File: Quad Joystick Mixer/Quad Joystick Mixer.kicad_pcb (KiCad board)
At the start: 2 copper layers, 55 x 96.8 mm, 59 parts, among them J1 B6B-XH-A, J2 Barrel_Jack_Switch, SW1 SW_DPDT_x2, U1 LM338-TO-220, U2 LM2990T-12/NOPB, U3 AP63200WU

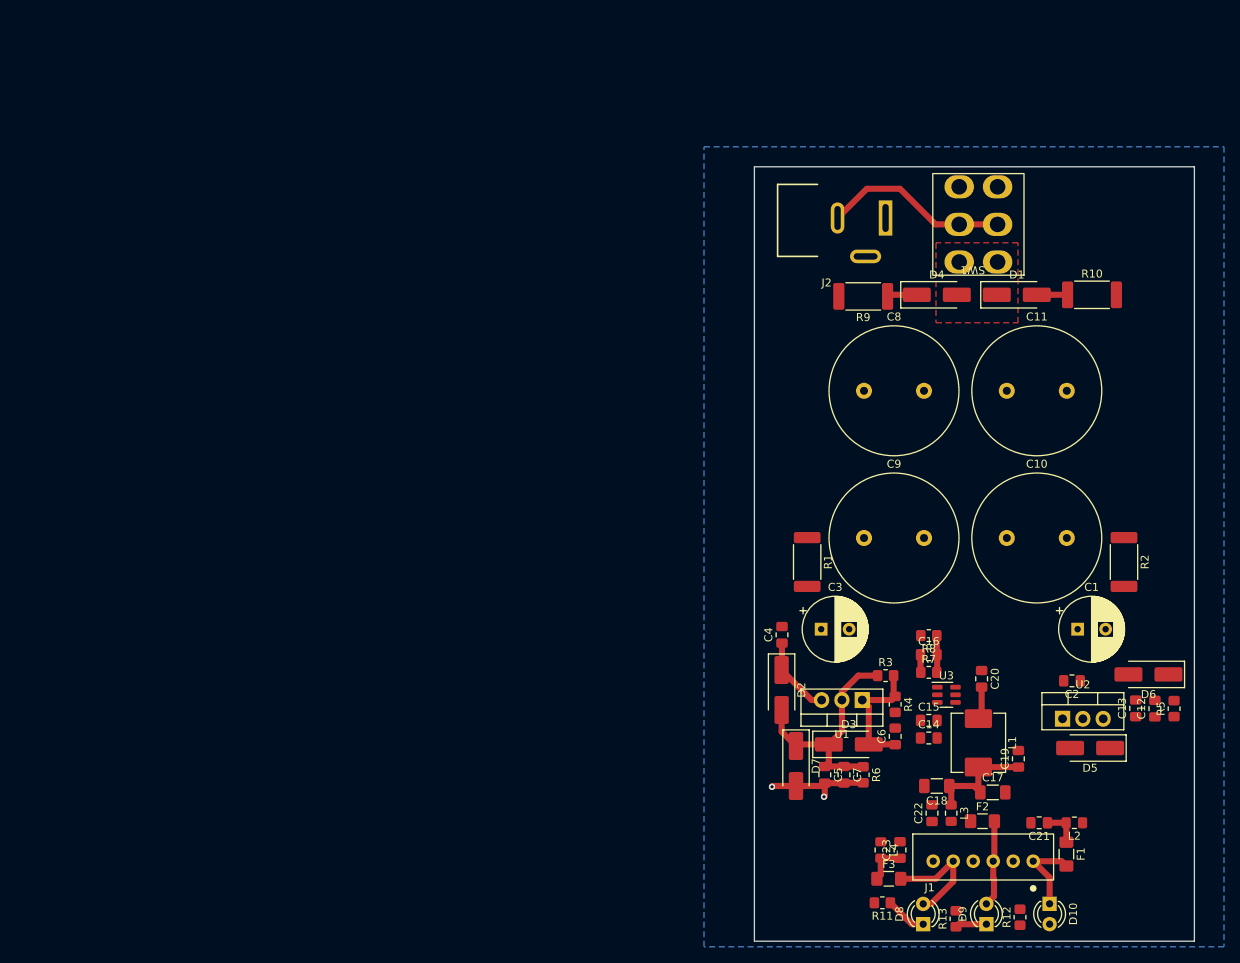
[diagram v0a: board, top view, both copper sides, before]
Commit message: clean up power supply schematic
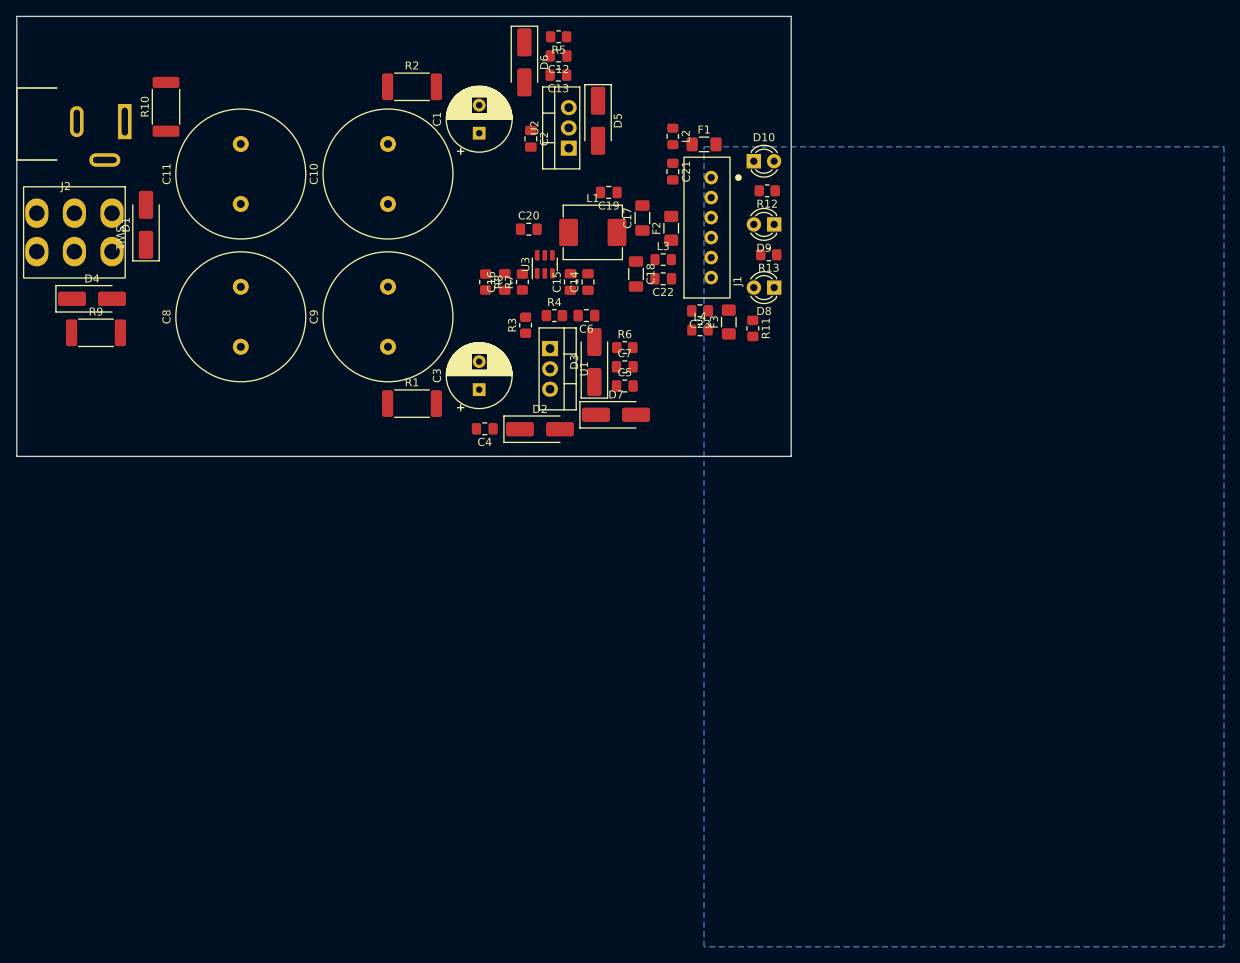
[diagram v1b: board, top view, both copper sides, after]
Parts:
- moved R10 118.1 mm to (55.2, 42.5), turned to 90 degrees
- moved R5 113.9 mm to (104.3, 33.7), turned to 180 degrees
- moved SW1 113.0 mm to (43.8, 58.2), turned to -90 degrees
- moved C12 110.5 mm to (104.3, 36.1), turned to 180 degrees
- moved D6 109.3 mm to (100.1, 36.9), turned to -90 degrees
- moved D1 109.2 mm to (52.8, 57.2), turned to 90 degrees
- moved C13 107.1 mm to (104.3, 38.5), turned to 180 degrees
- moved R2 107.0 mm to (86.0, 40.0), turned to 0 degrees
- moved D4 105.6 mm to (46.0, 66.5)
- moved D10 99.9 mm to (128.7, 49.3), turned to 0 degrees
- moved D5 99.7 mm to (109.3, 44.2), turned to -90 degrees
- moved F1 99.6 mm to (122.5, 47.2), turned to 0 degrees
- moved L2 99.4 mm to (118.6, 46.2), turned to -90 degrees
- moved C11 98.6 mm to (64.6, 54.6), turned to 90 degrees
- moved C1 97.2 mm to (94.4, 45.8), turned to 90 degrees
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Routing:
- net +12V: track 29.8 -> 0.00 mm
- net Net-(SW1A-B): track 23.4 -> 0.00 mm
- net +5V: track 17.2 -> 0.00 mm
- net Net-(D3-A): track 16.2 -> 0.00 mm
- net Net-(D8-A): track 14.9 -> 0.00 mm
- net Earth: track 13.4 -> 0.00 mm, vias 2 -> 0
- net Net-(D9-A): track 10.8 -> 0.00 mm
- net Net-(D10-K): track 10.6 -> 0.00 mm
- net Net-(D2-K): track 9.94 -> 0.00 mm
- net Net-(D8-K): track 5.21 -> 0.00 mm
- net Net-(C23-Pad1): track 5.18 -> 0.00 mm
- net Net-(C21-Pad1): track 4.77 -> 0.00 mm
- net Net-(U3-FB): track 4.63 -> 0.00 mm
- net Net-(U3-SW): track 4.10 -> 0.00 mm
- net Net-(D9-K): track 3.93 -> 0.00 mm
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- removed copper zone on F.Cu, net Net-(D1-K)
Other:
- board size 55 x 96.8 mm -> 96.8 x 55 mm

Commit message: work on placement and layout
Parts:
- removed F1, F2, F3: Polyfuse, Fuse:Fuse_1206_3216Metric_Pad1.42x1.75mm_HandSolder
- removed L1: 10uH, Inductor_SMD:L_Abracon_ASPI-0630LR
- removed L2, L3: L_Ferrite, Inductor_SMD:L_0805_2012Metric_Pad1.15x1.40mm_HandSolder
- added C24: 1uF, Capacitor_SMD:C_0805_2012Metric_Pad1.18x1.45mm_HandSolder, F.Cu at (313.4, 83.0)
- added C25: 10pF, Capacitor_SMD:C_0805_2012Metric_Pad1.18x1.45mm_HandSolder, F.Cu at (334.9, 66.5)
- added C26: 10uF, Capacitor_SMD:C_0805_2012Metric_Pad1.18x1.45mm_HandSolder, F.Cu at (330.3, 74.7)
- added C27: 10pF, Capacitor_SMD:C_0805_2012Metric_Pad1.18x1.45mm_HandSolder, F.Cu at (346.4, 61.5)
- added C28: 1uF, Capacitor_SMD:C_0805_2012Metric_Pad1.18x1.45mm_HandSolder, F.Cu at (358.4, 85.0)
- added C29: 10uF, Capacitor_SMD:C_0805_2012Metric_Pad1.18x1.45mm_HandSolder, F.Cu at (338.8, 77.1)
- added C30: 0.1uF, Capacitor_SMD:C_0805_2012Metric_Pad1.18x1.45mm_HandSolder, F.Cu at (334.3, 77.1)
- added C31: 0.1uF, Capacitor_SMD:C_0805_2012Metric_Pad1.18x1.45mm_HandSolder, F.Cu at (338.3, 68.1)
- added C32: 1uF, Capacitor_SMD:C_0805_2012Metric_Pad1.18x1.45mm_HandSolder, F.Cu at (335.5, 121.9)
- added C33: 1uF, Capacitor_SMD:C_0805_2012Metric_Pad1.18x1.45mm_HandSolder, F.Cu at (338.0, 131.4)
- added C34: 0.1uF, Capacitor_SMD:C_0805_2012Metric_Pad1.18x1.45mm_HandSolder, F.Cu at (-151.1, 101.3)
- added C35: 0.1uF, Capacitor_SMD:C_0805_2012Metric_Pad1.18x1.45mm_HandSolder, F.Cu at (-151.1, 104.3)
- added C36: 0.1uF, Capacitor_SMD:C_0805_2012Metric_Pad1.18x1.45mm_HandSolder, F.Cu at (-151.1, 107.3)
- added C37: 1uF, Capacitor_SMD:C_0805_2012Metric_Pad1.18x1.45mm_HandSolder, F.Cu at (-146.3, 92.3)
- added C38: 0.1uF, Capacitor_SMD:C_0805_2012Metric_Pad1.18x1.45mm_HandSolder, F.Cu at (-146.3, 95.3)
- added C39: 0.1uF, Capacitor_SMD:C_0805_2012Metric_Pad1.18x1.45mm_HandSolder, F.Cu at (-146.3, 98.3)
- added C40: 0.1uF, Capacitor_SMD:C_0805_2012Metric_Pad1.18x1.45mm_HandSolder, F.Cu at (-146.3, 101.3)
- added C41: 0.1uF, Capacitor_SMD:C_0805_2012Metric_Pad1.18x1.45mm_HandSolder, F.Cu at (-146.3, 104.3)
- added C42: 0.1uF, Capacitor_SMD:C_0805_2012Metric_Pad1.18x1.45mm_HandSolder, F.Cu at (-146.3, 107.3)
- added C43: 0.1uF, Capacitor_SMD:C_0805_2012Metric_Pad1.18x1.45mm_HandSolder, F.Cu at (138.6, 31.3)
- added C44: 0.1uF, Capacitor_SMD:C_0805_2012Metric_Pad1.18x1.45mm_HandSolder, F.Cu at (141.6, 31.3)
- added C45: 1uF, Capacitor_SMD:C_0805_2012Metric_Pad1.18x1.45mm_HandSolder, F.Cu at (-141.5, 92.3)
- added C46: 1uF, Capacitor_SMD:C_0805_2012Metric_Pad1.18x1.45mm_HandSolder, F.Cu at (-141.5, 95.3)
- added C47: 1uF, Capacitor_SMD:C_0805_2012Metric_Pad1.18x1.45mm_HandSolder, F.Cu at (-141.5, 98.3)
- added C48: 1uF, Capacitor_SMD:C_0805_2012Metric_Pad1.18x1.45mm_HandSolder, F.Cu at (-141.5, 101.3)
- added C49: 330pF, Capacitor_SMD:C_0805_2012Metric_Pad1.18x1.45mm_HandSolder, F.Cu at (144.6, 31.3)
- added C50: 330pF, Capacitor_SMD:C_0805_2012Metric_Pad1.18x1.45mm_HandSolder, F.Cu at (147.6, 31.3)
- added C51: 330pF, Capacitor_SMD:C_0805_2012Metric_Pad1.18x1.45mm_HandSolder, F.Cu at (150.6, 31.3)
- added C52: 330pF, Capacitor_SMD:C_0805_2012Metric_Pad1.18x1.45mm_HandSolder, F.Cu at (153.6, 31.3)
- added C53: 0.1uF, Capacitor_SMD:C_0805_2012Metric_Pad1.18x1.45mm_HandSolder, F.Cu at (156.6, 31.3)
- added C54: 0.1uF, Capacitor_SMD:C_0805_2012Metric_Pad1.18x1.45mm_HandSolder, F.Cu at (159.6, 31.3)
- added C55: 1uF, Capacitor_SMD:C_0805_2012Metric_Pad1.18x1.45mm_HandSolder, F.Cu at (-151.1, 127.1)
- added C56: 0.1uF, Capacitor_SMD:C_0805_2012Metric_Pad1.18x1.45mm_HandSolder, F.Cu at (-61.5, 185.0)
- added C57: 0.1uF, Capacitor_SMD:C_0805_2012Metric_Pad1.18x1.45mm_HandSolder, F.Cu at (-61.5, 182.5)
- added C58: 1uF, Capacitor_SMD:C_0805_2012Metric_Pad1.18x1.45mm_HandSolder, F.Cu at (-151.1, 136.1)
- added C59: 1uF, Capacitor_SMD:C_0805_2012Metric_Pad1.18x1.45mm_HandSolder, F.Cu at (-151.1, 139.1)
- added C60: 0.1uF, Capacitor_SMD:C_0805_2012Metric_Pad1.18x1.45mm_HandSolder, F.Cu at (-151.1, 142.1)
- added C61: 0.1uF, Capacitor_SMD:C_0805_2012Metric_Pad1.18x1.45mm_HandSolder, F.Cu at (-146.3, 127.1)
- added C62: 0.1uF, Capacitor_SMD:C_0805_2012Metric_Pad1.18x1.45mm_HandSolder, F.Cu at (-146.3, 130.1)
- added C63: 0.1uF, Capacitor_SMD:C_0805_2012Metric_Pad1.18x1.45mm_HandSolder, F.Cu at (-146.3, 133.1)
- added C64: 0.1uF, Capacitor_SMD:C_0805_2012Metric_Pad1.18x1.45mm_HandSolder, F.Cu at (-146.3, 136.1)
- added C65: 1uF, Capacitor_SMD:C_0805_2012Metric_Pad1.18x1.45mm_HandSolder, F.Cu at (-146.3, 139.1)
- added C66: 1uF, Capacitor_SMD:C_0805_2012Metric_Pad1.18x1.45mm_HandSolder, F.Cu at (-146.3, 142.1)
- added C67: 0.1uF, Capacitor_SMD:C_0805_2012Metric_Pad1.18x1.45mm_HandSolder, F.Cu at (-72.5, 199.0)
- added C68: 0.1uF, Capacitor_SMD:C_0805_2012Metric_Pad1.18x1.45mm_HandSolder, F.Cu at (-141.5, 130.1)
- added C69: 0.1uF, Capacitor_SMD:C_0805_2012Metric_Pad1.18x1.45mm_HandSolder, F.Cu at (-76.5, 207.0)
- added C70: 0.1uF, Capacitor_SMD:C_0805_2012Metric_Pad1.18x1.45mm_HandSolder, F.Cu at (-141.5, 136.1)
- added C71: 0.1uF, Capacitor_SMD:C_0805_2012Metric_Pad1.18x1.45mm_HandSolder, F.Cu at (51.6, 237.8)
- added C72: 0.1uF, Capacitor_SMD:C_0805_2012Metric_Pad1.18x1.45mm_HandSolder, F.Cu at (43.6, 233.8)
- added C73: 0.1uF, Capacitor_SMD:C_0805_2012Metric_Pad1.18x1.45mm_HandSolder, F.Cu at (39.5, 246.8)
- added C74: 0.1uF, Capacitor_SMD:C_0805_2012Metric_Pad1.18x1.45mm_HandSolder, F.Cu at (40.0, 232.3)
- added C75: 10uF, Capacitor_SMD:C_0805_2012Metric_Pad1.18x1.45mm_HandSolder, F.Cu at (42.5, 228.3)
- added C76: 10uF, Capacitor_SMD:C_0805_2012Metric_Pad1.18x1.45mm_HandSolder, F.Cu at (42.0, 242.8)
- added C77: 0.1uF, Capacitor_SMD:C_0805_2012Metric_Pad1.18x1.45mm_HandSolder, F.Cu at (113.2, 84.1)
- added C78: 0.1uF, Capacitor_SMD:C_0805_2012Metric_Pad1.18x1.45mm_HandSolder, F.Cu at (113.2, 88.3)
- added C80: 0.1uF, Capacitor_SMD:C_0805_2012Metric_Pad1.18x1.45mm_HandSolder, F.Cu at (100.9, 120.6)
- added C81: 0.1uF, Capacitor_SMD:C_0805_2012Metric_Pad1.18x1.45mm_HandSolder, F.Cu at (-8.68, 23.1)
- added C82: 0.1uF, Capacitor_SMD:C_0805_2012Metric_Pad1.18x1.45mm_HandSolder, F.Cu at (71.6, 224.0)
- added C83: 0.1uF, Capacitor_SMD:C_0805_2012Metric_Pad1.18x1.45mm_HandSolder, F.Cu at (93.6, 224.0)
- added C84: 0.1uF, Capacitor_SMD:C_0805_2012Metric_Pad1.18x1.45mm_HandSolder, F.Cu at (113.0, 224.0)
- added C85: 0.1uF, Capacitor_SMD:C_0805_2012Metric_Pad1.18x1.45mm_HandSolder, F.Cu at (109.0, 120.8)
- added C86: 0.1uF, Capacitor_SMD:C_0805_2012Metric_Pad1.18x1.45mm_HandSolder, F.Cu at (105.0, 121.5)
- added D11: LED, LED_THT:LED_D3.0mm_FlatTop, F.Cu at (-124.2, 38.0)
- added D12: MMSZ5222BT1G, Diode_SMD:D_SOD-123, F.Cu at (311.4, 73.5)
- added D13: MMSZ5222BT1G, Diode_SMD:D_SOD-123, F.Cu at (308.4, 73.5)
- added D14: MMSZ5222BT1G, Diode_SMD:D_SOD-123, F.Cu at (359.9, 71.0)
- added D15: MMSZ5222BT1G, Diode_SMD:D_SOD-123, F.Cu at (359.9, 76.5)
- added D16: BZT52C4V7-13-F, Diode_SMD:D_SOD-123, F.Cu at (-127.7, 118.1)
- added D17: BZT52C4V7-13-F, Diode_SMD:D_SOD-123, F.Cu at (-127.7, 152.9)
- added D18: DDZ9684-7, Diode_SMD:D_SOD-123, F.Cu at (52.0, 233.0)
- added D19: DDZ9684-7, Diode_SMD:D_SOD-123, F.Cu at (50.0, 241.3)
- added D20: LED, LED_THT:LED_D3.0mm_FlatTop, F.Cu at (-20.3, 68.7)
- added D21: LED, LED_THT:LED_D3.0mm_FlatTop, F.Cu at (-20.3, 74.2)
- added D22: SMAJ5.0A, Diode_SMD:D_SMA, F.Cu at (71.6, 227.0)
- added D23: SMAJ5.0A, Diode_SMD:D_SMA, F.Cu at (93.6, 227.0)
- added D24: SMAJ5.0A, Diode_SMD:D_SMA, F.Cu at (113.0, 227.0)
- added D25: SMAJ5.0A, Diode_SMD:D_SMA, F.Cu at (105.5, 54.7)
- added D26: SMAJ5.0A, Diode_SMD:D_SMA, F.Cu at (89.0, 55.0)
- added J3: NMJ6HCD, Eyewool Connectors:NMJ6HCD, F.Cu at (346.9, 103.0)
- added J4: NMJ6HCD, Eyewool Connectors:NMJ6HCD, F.Cu at (147.4, 37.3)
- added J5: NMJ6HCD, Eyewool Connectors:NMJ6HCD, F.Cu at (168.0, 37.3)
- added J6: NMJ6HCD, Eyewool Connectors:NMJ6HCD, F.Cu at (188.6, 37.3)
- added J7: NMJ6HCD, Eyewool Connectors:NMJ6HCD, F.Cu at (209.2, 37.3)
- added NT1: NetTie_2, NetTie:NetTie-2_SMD_Pad2.0mm, F.Cu at (-111.9, 131.3)
- added Q1: 2N7002, Package_TO_SOT_SMD:SOT-23, F.Cu at (-10.1, 68.1)
- added Q2: 2N7002, Package_TO_SOT_SMD:SOT-23, F.Cu at (-10.1, 72.6)
- added R14: 100k, Resistor_SMD:R_0805_2012Metric_Pad1.20x1.40mm_HandSolder, F.Cu at (310.9, 83.0)
- added R15: 4.7k, Resistor_SMD:R_0805_2012Metric_Pad1.20x1.40mm_HandSolder, F.Cu at (330.3, 70.6)
- added R16: 470, Resistor_SMD:R_0805_2012Metric_Pad1.20x1.40mm_HandSolder, F.Cu at (332.4, 66.5)
- added R17: 470, Resistor_SMD:R_0805_2012Metric_Pad1.20x1.40mm_HandSolder, F.Cu at (346.4, 64.0)
- added R18: 4.7k, Resistor_SMD:R_0805_2012Metric_Pad1.20x1.40mm_HandSolder, F.Cu at (359.4, 81.5)
- added R19: 100k, Resistor_SMD:R_0805_2012Metric_Pad1.20x1.40mm_HandSolder, F.Cu at (360.9, 85.0)
- added R20: 4.7R, Resistor_SMD:R_2010_5025Metric_Pad1.40x2.65mm_HandSolder, F.Cu at (335.0, 132.9)
- added R21: 10k, Resistor_SMD:R_0805_2012Metric_Pad1.20x1.40mm_HandSolder, F.Cu at (339.2, 128.2)
- added R22: 10k, Resistor_SMD:R_0805_2012Metric_Pad1.20x1.40mm_HandSolder, F.Cu at (339.2, 124.4)
- added R23: 20k, Resistor_SMD:R_0805_2012Metric_Pad1.20x1.40mm_HandSolder, F.Cu at (-151.1, 113.3)
- added R24: 100k, Resistor_SMD:R_0805_2012Metric_Pad1.20x1.40mm_HandSolder, F.Cu at (-151.1, 116.2)
- added R25: 10k, Resistor_SMD:R_0805_2012Metric_Pad1.20x1.40mm_HandSolder, F.Cu at (-151.1, 119.2)
- added R26: 10k, Resistor_SMD:R_0805_2012Metric_Pad1.20x1.40mm_HandSolder, F.Cu at (-151.1, 122.1)
- added R27: 10k, Resistor_SMD:R_0805_2012Metric_Pad1.20x1.40mm_HandSolder, F.Cu at (-146.4, 110.3)
- added R28: 100k, Resistor_SMD:R_0805_2012Metric_Pad1.20x1.40mm_HandSolder, F.Cu at (-146.4, 113.3)
- added R29: 100k, Resistor_SMD:R_0805_2012Metric_Pad1.20x1.40mm_HandSolder, F.Cu at (-146.4, 116.2)
- added R30: 100k, Resistor_SMD:R_0805_2012Metric_Pad1.20x1.40mm_HandSolder, F.Cu at (-146.4, 119.2)
- added R31: 100k, Resistor_SMD:R_0805_2012Metric_Pad1.20x1.40mm_HandSolder, F.Cu at (-146.4, 122.1)
- added R32: 20k, Resistor_SMD:R_0805_2012Metric_Pad1.20x1.40mm_HandSolder, F.Cu at (162.6, 31.4)
- added R33: 20k, Resistor_SMD:R_0805_2012Metric_Pad1.20x1.40mm_HandSolder, F.Cu at (165.6, 31.4)
- added R34: 1k, Resistor_SMD:R_0805_2012Metric_Pad1.20x1.40mm_HandSolder, F.Cu at (168.5, 31.4)
- added R35: 1k, Resistor_SMD:R_0805_2012Metric_Pad1.20x1.40mm_HandSolder, F.Cu at (171.5, 31.4)
- added R36: 20k, Resistor_SMD:R_0805_2012Metric_Pad1.20x1.40mm_HandSolder, F.Cu at (174.4, 31.4)
- added R37: 20k, Resistor_SMD:R_0805_2012Metric_Pad1.20x1.40mm_HandSolder, F.Cu at (177.4, 31.4)
- added R38: 1k, Resistor_SMD:R_0805_2012Metric_Pad1.20x1.40mm_HandSolder, F.Cu at (180.3, 31.4)
- added R39: 1k, Resistor_SMD:R_0805_2012Metric_Pad1.20x1.40mm_HandSolder, F.Cu at (183.3, 31.4)
- added R40: DNA, Resistor_SMD:R_2010_5025Metric_Pad1.40x2.65mm_HandSolder, F.Cu at (-111.5, 127.7)
- added R44: 10k, Resistor_SMD:R_0805_2012Metric_Pad1.20x1.40mm_HandSolder, F.Cu at (-141.6, 110.3)
- added R45: 10k, Resistor_SMD:R_0805_2012Metric_Pad1.20x1.40mm_HandSolder, F.Cu at (-141.6, 113.3)
- added R46: 10k, Resistor_SMD:R_0805_2012Metric_Pad1.20x1.40mm_HandSolder, F.Cu at (-141.6, 116.2)
- added R47: 10k, Resistor_SMD:R_0805_2012Metric_Pad1.20x1.40mm_HandSolder, F.Cu at (-141.6, 119.2)
- added R48: 100k, Resistor_SMD:R_0805_2012Metric_Pad1.20x1.40mm_HandSolder, F.Cu at (-151.1, 145.1)
- added R49: 10k, Resistor_SMD:R_0805_2012Metric_Pad1.20x1.40mm_HandSolder, F.Cu at (-151.1, 148.1)
- added R50: 100k, Resistor_SMD:R_0805_2012Metric_Pad1.20x1.40mm_HandSolder, F.Cu at (-151.1, 151.0)
- added R51: 10k, Resistor_SMD:R_0805_2012Metric_Pad1.20x1.40mm_HandSolder, F.Cu at (-61.5, 189.0)
- added R52: 10k, Resistor_SMD:R_0805_2012Metric_Pad1.20x1.40mm_HandSolder, F.Cu at (-151.1, 156.9)
- added R53: 100k, Resistor_SMD:R_0805_2012Metric_Pad1.20x1.40mm_HandSolder, F.Cu at (-146.4, 145.1)
- added R54: 20k, Resistor_SMD:R_0805_2012Metric_Pad1.20x1.40mm_HandSolder, F.Cu at (-146.4, 148.1)
- added R55: 20k, Resistor_SMD:R_0805_2012Metric_Pad1.20x1.40mm_HandSolder, F.Cu at (-146.4, 151.0)
- added R56: 10k, Resistor_SMD:R_0805_2012Metric_Pad1.20x1.40mm_HandSolder, F.Cu at (-146.4, 154.0)
- added R57: 10k, Resistor_SMD:R_0805_2012Metric_Pad1.20x1.40mm_HandSolder, F.Cu at (-146.4, 156.9)
- added R58: 100k, Resistor_SMD:R_0805_2012Metric_Pad1.20x1.40mm_HandSolder, F.Cu at (-141.6, 145.1)
- added R59: 10k, Resistor_SMD:R_0805_2012Metric_Pad1.20x1.40mm_HandSolder, F.Cu at (-141.6, 148.1)
- added R60: 10k, Resistor_SMD:R_0805_2012Metric_Pad1.20x1.40mm_HandSolder, F.Cu at (-141.6, 151.0)
- added R61: 100k, Resistor_SMD:R_0805_2012Metric_Pad1.20x1.40mm_HandSolder, F.Cu at (-141.6, 154.0)
- added R62: 1.43k, Resistor_SMD:R_0805_2012Metric_Pad1.20x1.40mm_HandSolder, F.Cu at (155.1, 243.3)
- added R63: 3.32k, Resistor_SMD:R_0805_2012Metric_Pad1.20x1.40mm_HandSolder, F.Cu at (151.1, 246.8)
- added R64: 100, Resistor_SMD:R_0805_2012Metric_Pad1.20x1.40mm_HandSolder, F.Cu at (40.0, 228.3)
- added R65: 100, Resistor_SMD:R_0805_2012Metric_Pad1.20x1.40mm_HandSolder, F.Cu at (39.5, 242.8)
- added R66: 4.7k, Resistor_SMD:R_0805_2012Metric_Pad1.20x1.40mm_HandSolder, F.Cu at (115.7, 100.8)
- added R67: 4.7k, Resistor_SMD:R_0805_2012Metric_Pad1.20x1.40mm_HandSolder, F.Cu at (115.7, 104.3)
- added R68: 4.7k, Resistor_SMD:R_0805_2012Metric_Pad1.20x1.40mm_HandSolder, F.Cu at (115.7, 107.8)
- added R69: 4.7k, Resistor_SMD:R_0805_2012Metric_Pad1.20x1.40mm_HandSolder, F.Cu at (115.7, 111.1)
- added R72: 10k, Resistor_SMD:R_0805_2012Metric_Pad1.20x1.40mm_HandSolder, F.Cu at (-19.6, 61.5)
- added R73: 6.04k, Resistor_SMD:R_0805_2012Metric_Pad1.20x1.40mm_HandSolder, F.Cu at (143.6, 248.3)
- added R74: 10k, Resistor_SMD:R_0805_2012Metric_Pad1.20x1.40mm_HandSolder, F.Cu at (135.6, 243.8)
- added R75: 16.5k, Resistor_SMD:R_0805_2012Metric_Pad1.20x1.40mm_HandSolder, F.Cu at (134.1, 236.3)
- added R76: 30.1k, Resistor_SMD:R_0805_2012Metric_Pad1.20x1.40mm_HandSolder, F.Cu at (138.1, 227.3)
- added R77: 71.5k, Resistor_SMD:R_0805_2012Metric_Pad1.20x1.40mm_HandSolder, F.Cu at (152.1, 227.8)
- added R78: 200, Resistor_SMD:R_0805_2012Metric_Pad1.20x1.40mm_HandSolder, F.Cu at (-14.8, 61.5)
- added R79: 10k, Resistor_SMD:R_0805_2012Metric_Pad1.20x1.40mm_HandSolder, F.Cu at (-14.8, 64.4)
- added R80: 200, Resistor_SMD:R_0805_2012Metric_Pad1.20x1.40mm_HandSolder, F.Cu at (-10.1, 49.7)
- added R81: 10k, Resistor_SMD:R_0805_2012Metric_Pad1.20x1.40mm_HandSolder, F.Cu at (-10.1, 52.6)
- added R82: 10k, Resistor_SMD:R_0805_2012Metric_Pad1.20x1.40mm_HandSolder, F.Cu at (75.1, 223.0)
- added R83: 10k, Resistor_SMD:R_0805_2012Metric_Pad1.20x1.40mm_HandSolder, F.Cu at (97.1, 223.0)
- added R84: 10k, Resistor_SMD:R_0805_2012Metric_Pad1.20x1.40mm_HandSolder, F.Cu at (116.5, 223.0)
- added R85: DNA, Resistor_SMD:R_0805_2012Metric_Pad1.20x1.40mm_HandSolder, F.Cu at (-117.8, 127.1)
- added R86: DNA, Resistor_SMD:R_0805_2012Metric_Pad1.20x1.40mm_HandSolder, F.Cu at (-117.8, 130.0)
- added R87: DNA, Resistor_SMD:R_0805_2012Metric_Pad1.20x1.40mm_HandSolder, F.Cu at (-117.8, 133.0)
- added R88: DNA, Resistor_SMD:R_0805_2012Metric_Pad1.20x1.40mm_HandSolder, F.Cu at (-117.8, 135.9)
- added RV1: 500kA, Eyewool Pots:StomboxParts_9MM, F.Cu at (321.9, 71.5)
- added RV2: 500kA, Eyewool Pots:StomboxParts_9MM, F.Cu at (349.4, 72.0)
- added RV3: 10k-B, Eyewool Pots:StomboxParts_9MM, F.Cu at (31.5, 225.3)
- added RV4: 10k-B, Eyewool Pots:StomboxParts_9MM, F.Cu at (31.5, 240.1)
- added SW2: Stompbox 1P8T Rotary, Eyewool Switches:Stompbox 1P8T Rotary, F.Cu at (145.0, 236.8)
- added SW3: Cherry MX, Button_Switch_Keyboard:SW_Cherry_MX_1.00u_PCB, F.Cu at (77.1, 234.0)
- added SW4: Cherry MX, Button_Switch_Keyboard:SW_Cherry_MX_1.00u_PCB, F.Cu at (98.5, 233.9)
- added SW5: Cherry MX, Button_Switch_Keyboard:SW_Cherry_MX_1.00u_PCB, F.Cu at (119.0, 233.9)
- added SW6: Cherry MX, Button_Switch_Keyboard:SW_Cherry_MX_1.00u_PCB, F.Cu at (111.1, 45.5)
- added SW7: Cherry MX, Button_Switch_Keyboard:SW_Cherry_MX_1.00u_PCB, F.Cu at (90.1, 45.5)
- added TP1: TestPoint, TestPoint:TestPoint_THTPad_D1.5mm_Drill0.7mm, F.Cu at (115.9, 89.3)
- added TP10: TestPoint, TestPoint:TestPoint_THTPad_D1.5mm_Drill0.7mm, F.Cu at (-128.8, 107.6)
- added TP11: TestPoint, TestPoint:TestPoint_THTPad_D1.5mm_Drill0.7mm, F.Cu at (-128.8, 142.4)
- added TP12: TestPoint, TestPoint:TestPoint_THTPad_D1.5mm_Drill0.7mm, F.Cu at (-128.8, 111.1)
- added TP13: TestPoint, TestPoint:TestPoint_THTPad_D1.5mm_Drill0.7mm, F.Cu at (-128.8, 145.9)
- added TP14: TestPoint, TestPoint:TestPoint_THTPad_D1.5mm_Drill0.7mm, F.Cu at (-128.8, 114.7)
- added TP15: TestPoint, TestPoint:TestPoint_THTPad_D1.5mm_Drill0.7mm, F.Cu at (-128.8, 149.5)
- added TP16: TestPoint, TestPoint:TestPoint_THTPad_D1.5mm_Drill0.7mm, F.Cu at (162.9, 27.2)
- added TP17: TestPoint, TestPoint:TestPoint_THTPad_D1.5mm_Drill0.7mm, F.Cu at (166.5, 27.2)
- added TP18: TestPoint, TestPoint:TestPoint_THTPad_D1.5mm_Drill0.7mm, F.Cu at (170.0, 27.2)
- added TP19: TestPoint, TestPoint:TestPoint_THTPad_D1.5mm_Drill0.7mm, F.Cu at (173.6, 27.2)
- added TP2: TestPoint, TestPoint:TestPoint_THTPad_D1.5mm_Drill0.7mm, F.Cu at (-131.1, 45.9)
- added TP20: TestPoint, TestPoint:TestPoint_THTPad_D1.5mm_Drill0.7mm, F.Cu at (52.0, 228.8)
- added TP21: TestPoint, TestPoint:TestPoint_THTPad_D1.5mm_Drill0.7mm, F.Cu at (48.0, 244.3)
- added TP22: TestPoint, TestPoint:TestPoint_THTPad_D1.5mm_Drill0.7mm, F.Cu at (-14.3, 74.8)
- added TP3: TestPoint, TestPoint:TestPoint_THTPad_D1.5mm_Drill0.7mm, F.Cu at (-110.0, 55.8)
- added TP4: TestPoint, TestPoint:TestPoint_THTPad_D1.5mm_Drill0.7mm, F.Cu at (-110.0, 59.3)
- added TP5: TestPoint, TestPoint:TestPoint_THTPad_D1.5mm_Drill0.7mm, F.Cu at (-110.0, 62.9)
- added TP6: TestPoint, TestPoint:TestPoint_THTPad_D1.5mm_Drill0.7mm, F.Cu at (309.9, 69.0)
- added TP7: TestPoint, TestPoint:TestPoint_THTPad_D1.5mm_Drill0.7mm, F.Cu at (359.9, 66.5)
- added TP8: TestPoint, TestPoint:TestPoint_THTPad_D1.5mm_Drill0.7mm, F.Cu at (-128.8, 104.0)
- added TP9: TestPoint, TestPoint:TestPoint_THTPad_D1.5mm_Drill0.7mm, F.Cu at (-128.8, 138.8)
- added U10: TL072, Package_SO:SOIC-8_3.9x4.9mm_P1.27mm, F.Cu at (-134.8, 118.4)
- added U11: TL072, Package_SO:SOIC-8_3.9x4.9mm_P1.27mm, F.Cu at (188.0, 29.5)
- added U12: TL072, Package_SO:SOIC-8_3.9x4.9mm_P1.27mm, F.Cu at (194.4, 29.5)
- added U13: DS1881Z-050+, Package_SO:SOIC-16_3.9x9.9mm_P1.27mm, F.Cu at (-68.0, 188.4)
- added U14: TL072, Package_SO:SOIC-8_3.9x4.9mm_P1.27mm, F.Cu at (-134.8, 140.3)
- added U15: TL072, Package_SO:SOIC-8_3.9x4.9mm_P1.27mm, F.Cu at (-74.5, 203.1)
- added U16: TL072, Package_SO:SOIC-8_3.9x4.9mm_P1.27mm, F.Cu at (-134.8, 153.2)
- added U17: DS1881Z-050+, Package_SO:SOIC-16_3.9x9.9mm_P1.27mm, F.Cu at (-126.4, 131.3)
- added U19: TL072, Package_SO:SOIC-8_3.9x4.9mm_P1.27mm, F.Cu at (47.6, 235.8)
- added U20: Teensy4.0, teensy:Teensy40, F.Cu at (102.5, 101.0)
- added U4: TL072, Package_SO:SOIC-8_3.9x4.9mm_P1.27mm, F.Cu at (336.4, 72.5)
- added U5: MCP1755T-5002E/OT, Package_TO_SOT_SMD:SOT-23-5_HandSoldering, F.Cu at (335.2, 125.9)
- added U6: TL072, Package_SO:SOIC-8_3.9x4.9mm_P1.27mm, F.Cu at (-134.8, 105.5)
- added U7: TL072, Package_SO:SOIC-8_3.9x4.9mm_P1.27mm, F.Cu at (-134.8, 111.9)
- added U8: DS1881Z-050+, Package_SO:SOIC-16_3.9x9.9mm_P1.27mm, F.Cu at (-134.8, 96.5)
- added U9: DS1881Z-050+, Package_SO:SOIC-16_3.9x9.9mm_P1.27mm, F.Cu at (-126.4, 96.5)
- C1: value 100uF -> 10uF; footprint Capacitor_THT:CP_Radial_D8.0mm_P3.50mm -> Capacitor_SMD:C_0805_2012Metric_Pad1.18x1.45mm_HandSolder
- C10: value 2200uF -> 10uF; footprint Capacitor_THT:C_Radial_D16.0mm_H25.0mm_P7.50mm -> Capacitor_SMD:C_0805_2012Metric_Pad1.18x1.45mm_HandSolder
- C11, C8, C9: value 2200uF -> 0.1uF; footprint Capacitor_THT:C_Radial_D16.0mm_H25.0mm_P7.50mm -> Capacitor_SMD:C_0805_2012Metric_Pad1.18x1.45mm_HandSolder
- C12: value 10uF -> 2200uF; footprint Capacitor_SMD:C_0805_2012Metric_Pad1.18x1.45mm_HandSolder -> Capacitor_THT:C_Radial_D16.0mm_H25.0mm_P7.50mm
- C13: value 0.1uF -> 2200uF; footprint Capacitor_SMD:C_0805_2012Metric_Pad1.18x1.45mm_HandSolder -> Capacitor_THT:C_Radial_D16.0mm_H25.0mm_P7.50mm
- C14, C5: value 10uF -> 100uF; footprint Capacitor_SMD:C_0805_2012Metric_Pad1.18x1.45mm_HandSolder -> Capacitor_THT:CP_Radial_D8.0mm_P3.50mm
- C15: value 0.1uF -> 1uF
- C16: value 100pF -> 0.1uF
- C2: value 1uF -> 0.1uF
- C21, C7: value 0.1uF -> 10uF
- C23: value 0.1uF -> 100pF
- C3: value 100uF -> 2200uF; footprint Capacitor_THT:CP_Radial_D8.0mm_P3.50mm -> Capacitor_THT:C_Radial_D16.0mm_H25.0mm_P7.50mm
- C4: value 1uF -> 2200uF; footprint Capacitor_SMD:C_0805_2012Metric_Pad1.18x1.45mm_HandSolder -> Capacitor_THT:C_Radial_D16.0mm_H25.0mm_P7.50mm
- C6: value 10uF -> 1uF
- D10: value LED -> B350; footprint LED_THT:LED_D3.0mm_FlatTop -> Diode_SMD:D_SMA_Handsoldering
- D7: value B350 -> LED; footprint Diode_SMD:D_SMA_Handsoldering -> LED_THT:LED_D3.0mm_FlatTop
- J1: value B6B-XH-A -> Barrel_Jack_Switch; footprint Eyewool Connectors:B6B-XH-A -> Eyewool Connectors:Love My Switches 2.1MM PCB Mount DC Jack
- J2: value Barrel_Jack_Switch -> NMJ6HCD; footprint Eyewool Connectors:Love My Switches 2.1MM PCB Mount DC Jack -> Eyewool Connectors:NMJ6HCD
- L4: value L_Ferrite -> 10uH; footprint Inductor_SMD:L_0805_2012Metric_Pad1.15x1.40mm_HandSolder -> Inductor_SMD:L_Abracon_ASPI-0630LR
- R10: value 0.5R -> 3k; footprint Resistor_SMD:R_2512_6332Metric_Pad1.40x3.35mm_HandSolder -> Resistor_SMD:R_0805_2012Metric_Pad1.20x1.40mm_HandSolder
- R12: value 10k -> 158k
- R13: value 300 -> 30k
- R3: value 270R -> 3k
- R4: value 2.3k -> 270R
- R5: value 10k -> 2.32k
- R6: value 10k -> 0.5R; footprint Resistor_SMD:R_0805_2012Metric_Pad1.20x1.40mm_HandSolder -> Resistor_SMD:R_2512_6332Metric_Pad1.40x3.35mm_HandSolder
- R7: value 157k -> 0.5R; footprint Resistor_SMD:R_0805_2012Metric_Pad1.20x1.40mm_HandSolder -> Resistor_SMD:R_2512_6332Metric_Pad1.40x3.35mm_HandSolder
- R8: value 30k -> 20k
- R9: value 0.5R -> 10k; footprint Resistor_SMD:R_2512_6332Metric_Pad1.40x3.35mm_HandSolder -> Resistor_SMD:R_0805_2012Metric_Pad1.20x1.40mm_HandSolder
- moved J2 293.4 mm to (325.0, 103.0), turned to -90 degrees
- moved R11 262.6 mm to (-133.6, 85.8), turned to 0 degrees
- moved D8 258.3 mm to (-124.2, 26.9), turned to 0 degrees
- moved D9 256.7 mm to (-124.2, 32.5), turned to 0 degrees
- moved C16 251.0 mm to (-151.1, 98.3), turned to 0 degrees
- moved R8 250.6 mm to (-151.1, 110.3), turned to 0 degrees
- moved D7 243.1 mm to (-124.2, 21.4)
- moved C9 235.2 mm to (-151.1, 95.3), turned to 0 degrees
- moved R3 233.8 mm to (-133.6, 71.0), turned to 0 degrees
- moved C8 216.6 mm to (-151.1, 92.3), turned to 0 degrees
- moved R10 193.1 mm to (-133.6, 82.8), turned to 0 degrees
- moved R9 180.3 mm to (-133.6, 79.9)
- moved D10 109.5 mm to (39.7, 113.1), turned to 180 degrees
- moved D5 95.1 mm to (39.7, 109.1), turned to 0 degrees
- moved U2 83.7 mm to (43.0, 103.2), turned to 180 degrees
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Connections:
- C1 pad 1: Earth -> +12V
- C1 pad 2: Net-(D5-A) -> Earth
- C10 pad 1: Earth -> -12V
- C10 pad 2: Net-(C10-Pad2) -> Earth
- C11 pad 1: Earth -> -12V
- C11 pad 2: Net-(C10-Pad2) -> Earth
- C12 pad 1: -12V -> Earth
- C12 pad 2: Earth -> Net-(C12-Pad2)
- C13 pad 1: -12V -> Earth
- C13 pad 2: Earth -> Net-(C12-Pad2)
- C14 pad 1: +12V -> Earth
- C14 pad 2: Earth -> Net-(D5-A)
- C15 pad 1: +12V -> Net-(D5-A)
- C16 pad 1: +5V -> +12V
- C16 pad 2: Net-(U3-FB) -> GND
- C2 pad 1: Net-(D5-A) -> +12V
- C21 pad 1: Net-(C21-Pad1) -> +12V
- C22 pad 1: Net-(C22-Pad1) -> +12V
- C23 pad 1: Net-(C23-Pad1) -> +5V
- C23 pad 2: Earth -> Net-(U3-FB)
- C3 pad 1: Net-(D2-K) -> Net-(C3-Pad1)
- C4 pad 1: Net-(D2-K) -> Net-(C3-Pad1)
- C5 pad 1: +12V -> Net-(D1-K)
- C6 pad 1: Net-(D3-A) -> Net-(D1-K)
- C7 pad 1: +12V -> Net-(D3-A)
- C8 pad 1: Net-(C8-Pad1) -> +12V
- C8 pad 2: Earth -> GND
- C9 pad 1: Net-(C8-Pad1) -> -12V
- C9 pad 2: Earth -> GND
- D1 pad 2: Net-(D1-A) -> +12V
- D10 pad 1: Net-(D10-K) -> Earth
- D10 pad 2: Net-(D10-A) -> -12V
- D2 pad 2: +12V -> Net-(D2-A)
- D4 pad 1: Net-(D4-K) -> +12V
- D4 pad 2: Net-(D1-K) -> Earth
- D6 pad 1: Earth -> Net-(D2-A)
- D6 pad 2: -12V -> Net-(D6-A)
- D7 pad 1: +12V -> Net-(D7-K)
- D7 pad 2: Earth -> +12V
- D8 pad 2: Net-(D8-A) -> +5V
- D9 pad 1: Net-(D9-K) -> -12V
- J1 pad 1: Net-(D10-K) -> Earth
- J1 pad 2: Earth -> Net-(SW1A-B)
- J1 pad 3: Net-(D9-A) -> unconnected-(J1-Pad3)
- L4 pad 1: +12V -> Net-(U3-SW)
- L4 pad 2: Net-(C23-Pad1) -> +5V
- R1 pad 1: Net-(C8-Pad1) -> Net-(D2-K)
- R1 pad 2: Net-(D2-K) -> Net-(C3-Pad1)
- R10 pad 1: Net-(D1-A) -> Net-(D8-K)
- R10 pad 2: Net-(C10-Pad2) -> Earth
- R11 pad 1: Net-(D8-K) -> Net-(D9-A)
- R12 pad 1: Net-(D10-A) -> +5V
- R12 pad 2: Earth -> Net-(U3-FB)
- R13 pad 1: Net-(D9-K) -> Net-(U3-FB)
- R2 pad 1: Net-(C10-Pad2) -> Net-(C3-Pad1)
- R2 pad 2: Net-(D5-A) -> Net-(D1-K)
- R3 pad 1: +12V -> Net-(D11-K)
- R3 pad 2: Net-(D3-A) -> Earth
- R4 pad 1: Net-(D3-A) -> +12V
- R4 pad 2: Earth -> Net-(D3-A)
- R5 pad 1: -12V -> Net-(D3-A)
- R6 pad 1: +12V -> Net-(D6-A)
- R6 pad 2: Earth -> Net-(C12-Pad2)
- R7 pad 1: +5V -> Net-(C12-Pad2)
- R7 pad 2: Net-(U3-FB) -> Net-(D5-A)
- R8 pad 1: Net-(U3-FB) -> VCC
- R8 pad 2: Earth -> Net-(U7A-+)
- R9 pad 1: Net-(D4-K) -> Net-(D7-K)
- R9 pad 2: Net-(C8-Pad1) -> Earth
- SW1 pad 1: Net-(D1-K) -> Net-(D2-A)
- SW1 pad 4: Net-(D1-K) -> Net-(D2-A)
- U1 pad 3: Net-(D2-K) -> Net-(D1-K)
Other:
- board outline removed

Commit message: major layout progress
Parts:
- removed C61, C64: 0.1uF, Capacitor_SMD:C_0805_2012Metric_Pad1.18x1.45mm_HandSolder
- removed R54, R55: 20k, Resistor_SMD:R_0805_2012Metric_Pad1.20x1.40mm_HandSolder
- removed U15: TL072, Package_SO:SOIC-8_3.9x4.9mm_P1.27mm
- added TP23: TestPoint, TestPoint:TestPoint_THTPad_D1.5mm_Drill0.7mm, F.Cu at (178.7, 113.6)
- moved R52 399.4 mm to (241.9, 85.4), turned to 180 degrees
- moved C59 393.0 mm to (237.8, 82.9)
- moved R53 388.8 mm to (237.9, 85.4), turned to 180 degrees
- moved R50 383.0 mm to (225.3, 80.4)
- moved C58 380.2 mm to (225.3, 82.9), turned to 180 degrees
- moved R49 378.5 mm to (221.9, 83.9), turned to 90 degrees
- moved R48 372.9 mm to (220.7, 117.0), turned to -90 degrees
- moved C55 372.9 mm to (221.7, 120.3), turned to 180 degrees
- moved U14 371.0 mm to (231.8, 83.4)
- moved TP11 368.7 mm to (237.3, 99.2)
- moved C66 363.8 mm to (212.7, 83.1)
- moved C63 361.2 mm to (212.8, 93.8)
- moved R61 360.9 mm to (212.7, 85.6), turned to 180 degrees
- moved C62 360.6 mm to (212.8, 96.3)
- moved R60 359.9 mm to (212.7, 88.1)
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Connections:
- net /Channel 1 Digital Pots/Mix_Input renamed Net-(D16-K)
- net /Channel 2 Digital Pots/Mix_Input renamed Net-(D17-K)
- C32 pad 2: Earth -> GND
- C33 pad 2: Earth -> GND
- C34 pad 1: -12V -> VCC
- C36 pad 1: VCC -> -12V
- C38 pad 2: Earth -> GND
- C40 pad 2: Earth -> GND
- C57 pad 2: Earth -> GND
- C60 pad 1: VCC -> VDD
- C63 pad 2: Earth -> GND
- R20 pad 1: +12V -> Net-(U5-VIN)
- R20 pad 2: Net-(U5-VIN) -> +12V
- R25 pad 2: Earth -> GND
- R26 pad 2: Earth -> GND
- R3 pad 2: Earth -> GND
- R38 pad 1: Net-(J6-PadT) -> Net-(J7-PadT)
- R39 pad 1: Net-(J7-PadT) -> Net-(J6-PadT)
- R51 pad 2: Earth -> GND
- R59 pad 2: Earth -> GND
- TP18 pad 1: Net-(J6-PadT) -> Net-(J7-PadT)
- TP19 pad 1: Net-(J7-PadT) -> Net-(J6-PadT)
- U13 pad 2: Earth -> GND
- U13 pad 3: Earth -> GND
- U13 pad 5: Earth -> GND
- U17 pad 2: Earth -> GND
- U17 pad 3: Earth -> GND
- U5 pad 2: Earth -> GND
- U8 pad 2: Earth -> GND
- U8 pad 3: Earth -> GND
- U8 pad 5: Earth -> GND
- U9 pad 2: Earth -> GND
- U9 pad 3: Earth -> GND
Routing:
- net /Audio Output/D: track 0.00 -> 220.8 mm
- net /SDA1: track 0.00 -> 178.5 mm, vias 0 -> 3
- net +3.3V: track 0.00 -> 166.0 mm, vias 0 -> 12
- net /SCL1: track 0.00 -> 165.1 mm, vias 0 -> 3
- net /Audio Output/C: track 0.00 -> 148.6 mm
- net /Teensy/Button_1: track 0.00 -> 134.4 mm
- net /Audio Input/Channel2_Input: track 0.00 -> 133.3 mm
- net GND: track 0.00 -> 128.1 mm, vias 0 -> 66
- net /Teensy/Button_3: track 0.00 -> 119.1 mm
- net /Teensy/Button_2: track 0.00 -> 117.2 mm
- net Earth: track 0.00 -> 114.9 mm, vias 0 -> 54
- net /Audio Input/Channel1_Input: track 0.00 -> 107.2 mm
- net /Teensy/POWER: track 0.00 -> 96.6 mm
- net /SDA0: track 0.00 -> 93.8 mm, vias 0 -> 3
- net /SCL0: track 0.00 -> 91.2 mm, vias 0 -> 3
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- added copper zone on F.Cu, net +12V
- added copper zone on In2.Cu, net +12V
- added copper zone on In2.Cu, net +3.3V
- added copper zone on F.Cu, net +5V
- added copper zone on F.Cu, net -12V
- added copper zone on In2.Cu, net -12V
- added copper zone on F.Cu, net Earth
- added copper zone on In1.Cu, net Earth
- added copper zone on F.Cu, net GND
- added copper zone on In1.Cu, net GND
- added copper zone on F.Cu, net VCC
- added copper zone on In2.Cu, net VCC
- added copper zone on F.Cu, net VDD
- added copper zone on In2.Cu, net VDD
- removed copper zone on B.Cu, net Earth
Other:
- board outline added: 222 x 134.8 mm
- copper layers 2 -> 4

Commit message: more progress on layout
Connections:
- U20 pad 21: /Teensy/AB_Control -> /Teensy/Channel Selection
- U20 pad 22: /Teensy/CD_Control -> /Teensy/AB_Control
- U20 pad 27: /Teensy/Channel Selection -> /Teensy/CD_Control
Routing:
- net /Teensy/CD_Control: track 7.45 -> 153.4 mm
- net /Teensy/AB_Control: track 4.58 -> 112.9 mm
- net /Teensy/Channel Selection: track 19.3 -> 99.4 mm
- net Earth: track 114.9 -> 117.1 mm, vias 54 -> 56
- net -12V: track 43.0 -> 44.7 mm, vias 8 -> 9
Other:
- board size 222 x 134.8 mm -> 215 x 134.8 mm
